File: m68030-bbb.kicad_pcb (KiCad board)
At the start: 4 copper layers, 177.8 x 127 mm, 13 parts, among them U1 MC68030, U10 M29F160F, U11 M29F160F, U12 XC95108TQ100, U13 SST39SF010, U2 R68561, U3 68230, U4 CY62167GN-45ZXI, U5 CY62167GN-45ZXI, U6 CY62167GN-45ZXI, U7 CY62167GN-45ZXI, U8 M29F160F, U9 M29F160F

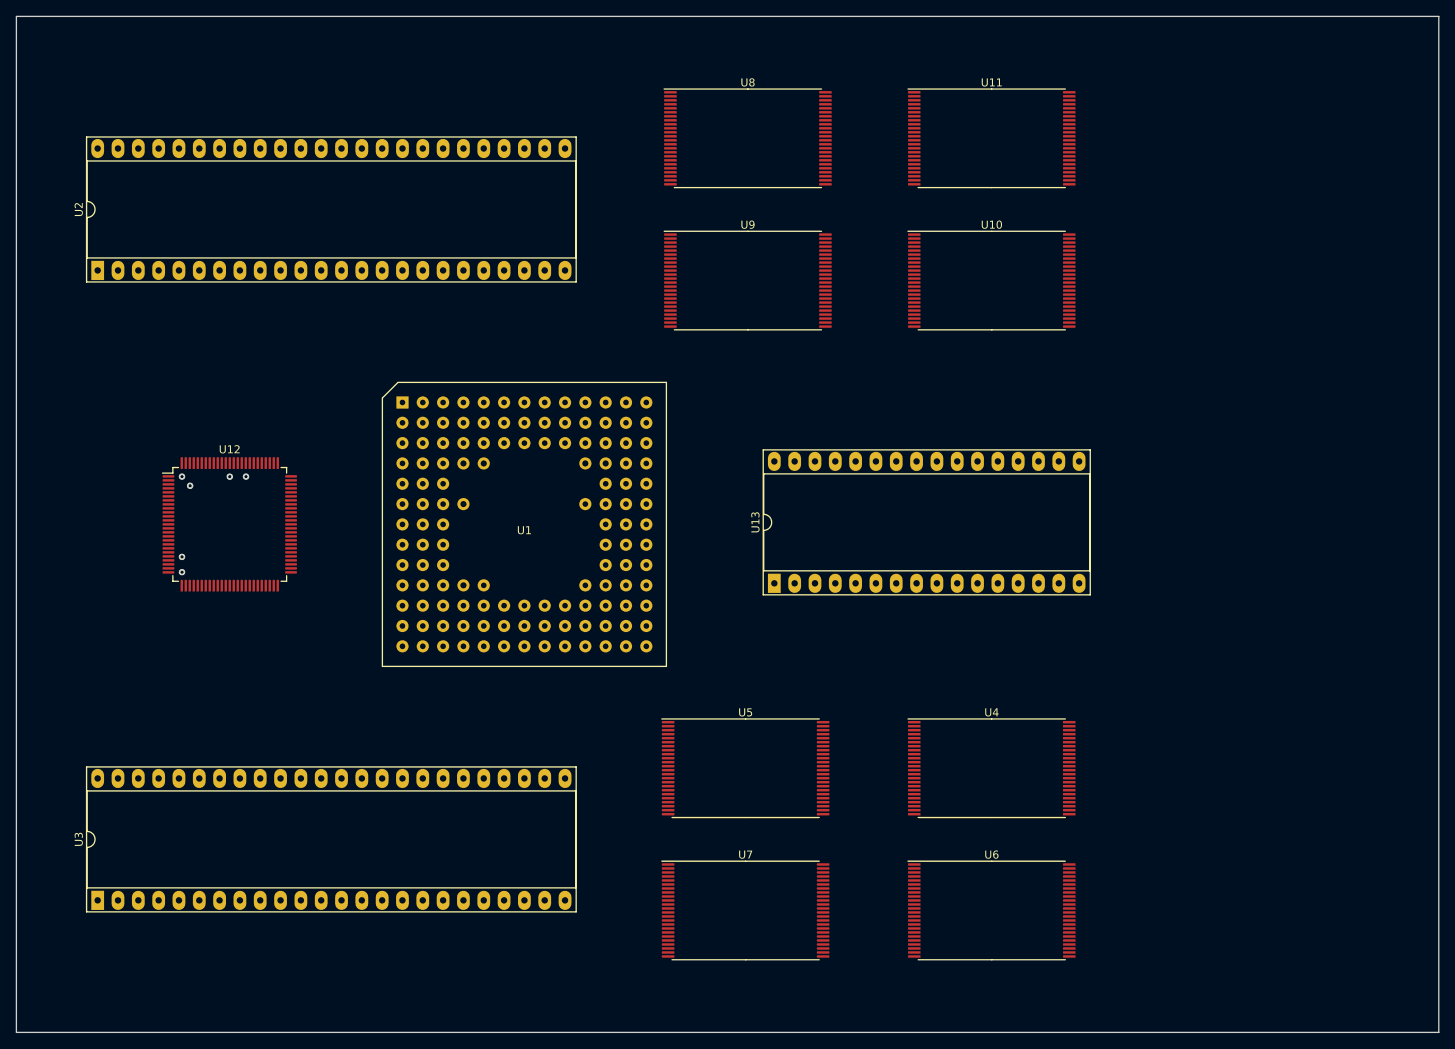
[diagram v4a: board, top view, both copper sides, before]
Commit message: Pretty much finished with the glue logic.  Doing intc now.
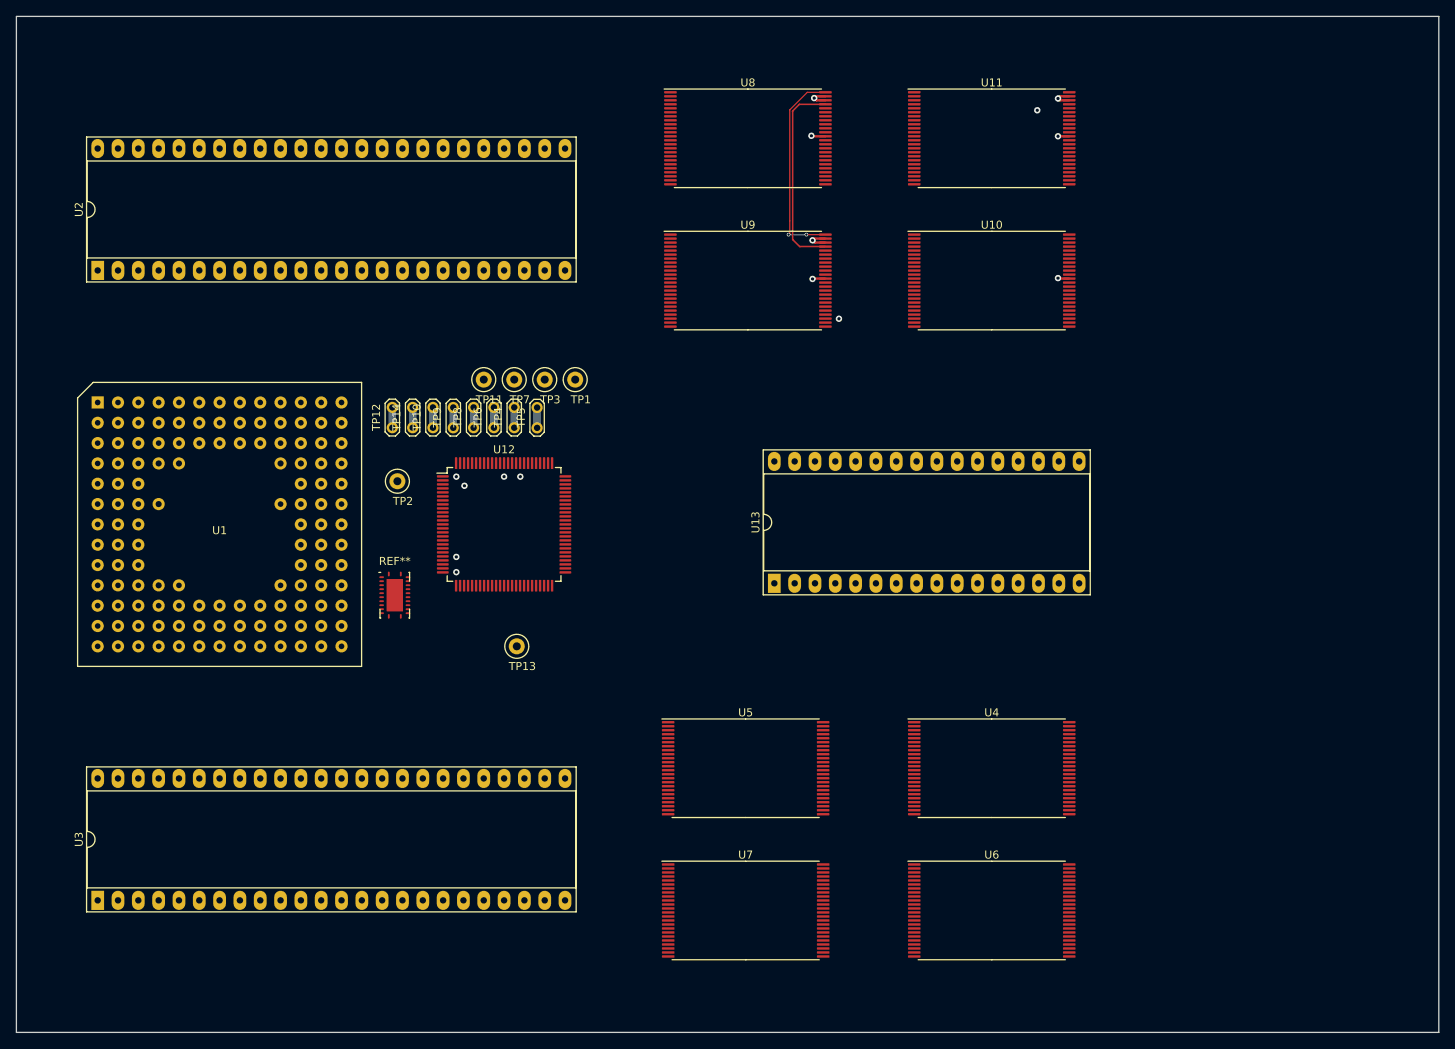
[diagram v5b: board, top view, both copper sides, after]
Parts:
- added REF**: VQFN-24_EP_3.4x5.4_Pitch0.5mm_RHL0024A, Rassilon:VQFN-24_EP_3.4x5.4_Pitch0.5mm_RHL0024A, F.Cu at (136.2, 91.4)
- added TP1: TestPoint_Small, TestPoint:TestPoint_Loop_D2.50mm_Drill1.0mm, F.Cu at (158.8, 64.5)
- added TP10: PGND, Rassilon:TestPoint_2Pads_Pitch2.54mm_Drill0.8mm_tie_bottom, F.Cu at (141.0, 70.5)
- added TP11: TestPoint_Small, TestPoint:TestPoint_Loop_D2.50mm_Drill1.0mm, F.Cu at (147.3, 64.5)
- added TP12: PGND, Rassilon:TestPoint_2Pads_Pitch2.54mm_Drill0.8mm_tie_bottom, F.Cu at (135.9, 70.5)
- added TP13: OCS, TestPoint:TestPoint_Loop_D2.50mm_Drill1.0mm, F.Cu at (151.4, 97.8)
- added TP14: PGND, Rassilon:TestPoint_2Pads_Pitch2.54mm_Drill0.8mm_tie_bottom, F.Cu at (138.4, 70.5)
- added TP2: TestPoint_Small, TestPoint:TestPoint_Loop_D2.50mm_Drill1.0mm, F.Cu at (136.5, 77.2)
- added TP3: PND, TestPoint:TestPoint_Loop_D2.50mm_Drill1.0mm, F.Cu at (154.9, 64.5)
- added TP4: PGND, Rassilon:TestPoint_2Pads_Pitch2.54mm_Drill0.8mm_tie_bottom, F.Cu at (151.1, 70.5)
- added TP5: PGND, Rassilon:TestPoint_2Pads_Pitch2.54mm_Drill0.8mm_tie_bottom, F.Cu at (154.0, 70.5)
- added TP6: PGND, Rassilon:TestPoint_2Pads_Pitch2.54mm_Drill0.8mm_tie_bottom, F.Cu at (148.6, 70.5)
- added TP7: TestPoint_Small, TestPoint:TestPoint_Loop_D2.50mm_Drill1.0mm, F.Cu at (151.1, 64.5)
- added TP8: PGND, Rassilon:TestPoint_2Pads_Pitch2.54mm_Drill0.8mm_tie_bottom, F.Cu at (146.1, 70.5)
- added TP9: PGND, Rassilon:TestPoint_2Pads_Pitch2.54mm_Drill0.8mm_tie_bottom, F.Cu at (143.5, 70.5)
- moved U1 38.1 mm to (114.3, 82.5)
- moved U12 34.3 mm to (149.9, 82.5)
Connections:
- net /SYSCLK2X renamed /~{CPUCLK}
- U10 pad 12: unconnected-(U10-Pad12) -> /~{RESET}
- U10 pad 37: unconnected-(U10-Pad37) -> +5V
- U10 pad 45: unconnected-(U10-Pad45) -> /A2
- U10 pad 47: unconnected-(U10-Pad47) -> GND
- U11 pad 12: unconnected-(U11-Pad12) -> /~{RESET}
- U11 pad 37: unconnected-(U11-Pad37) -> +5V
- U11 pad 45: unconnected-(U11-Pad45) -> /A2
- U11 pad 47: unconnected-(U11-Pad47) -> GND
- U12 pad 1: unconnected-(U12-Pad1) -> /~{RESET}
- U12 pad 11: unconnected-(U12-Pad11) -> /~{WR}
- U12 pad 12: unconnected-(U12-Pad12) -> /~{RD}
- U12 pad 15: /~{AS} -> /R/~{W}
- U12 pad 16: /~{DS} -> /~{CIIN}
- U12 pad 17: /R/~{W} -> /~{CIOUT}
- U12 pad 18: unconnected-(U12-Pad18) -> /~{DS}
- U12 pad 2: unconnected-(U12-Pad2) -> /~{IOSEL}
- U12 pad 23: /SYSCLK -> /~{AS}
- U12 pad 25: unconnected-(U12-Pad25) -> /A0
- U12 pad 28: unconnected-(U12-Pad28) -> /A1
- U12 pad 29: unconnected-(U12-Pad29) -> /~{RDUU}
- U12 pad 3: unconnected-(U12-Pad3) -> Net-(TP2-Pad1)
- U12 pad 30: unconnected-(U12-Pad30) -> /~{RDUM}
- U12 pad 32: unconnected-(U12-Pad32) -> /~{RDLM}
- U12 pad 33: unconnected-(U12-Pad33) -> /~{RDLL}
- U12 pad 34: unconnected-(U12-Pad34) -> /~{WEUU}
- U12 pad 35: unconnected-(U12-Pad35) -> /~{WEUM}
- U12 pad 36: unconnected-(U12-Pad36) -> /~{WELM}
- U12 pad 37: unconnected-(U12-Pad37) -> /~{WELL}
- U12 pad 39: unconnected-(U12-Pad39) -> /~{UDS}
- U12 pad 4: unconnected-(U12-Pad4) -> /~{IOSEL}
- U12 pad 40: unconnected-(U12-Pad40) -> /~{LDS}
- U12 pad 41: unconnected-(U12-Pad41) -> Net-(TP13-Pad1)
- U12 pad 42: unconnected-(U12-Pad42) -> /~{IOCS0}
- U12 pad 49: unconnected-(U12-Pad49) -> /~{IOCS1}
- U12 pad 65: unconnected-(U12-Pad65) -> /A20
- U12 pad 66: unconnected-(U12-Pad66) -> /A21
- U12 pad 67: unconnected-(U12-Pad67) -> /A22
- U12 pad 68: unconnected-(U12-Pad68) -> /A23
- U12 pad 70: unconnected-(U12-Pad70) -> /A24
- U12 pad 71: unconnected-(U12-Pad71) -> /A25
- U12 pad 72: unconnected-(U12-Pad72) -> /A26
- U12 pad 73: unconnected-(U12-Pad73) -> /A27
- U12 pad 74: unconnected-(U12-Pad74) -> /A28
- U12 pad 76: unconnected-(U12-Pad76) -> /A29
- U12 pad 77: unconnected-(U12-Pad77) -> /A30
- U12 pad 78: unconnected-(U12-Pad78) -> /A31
- U12 pad 79: unconnected-(U12-Pad79) -> Net-(TP1-Pad1)
- U12 pad 80: unconnected-(U12-Pad80) -> Net-(TP5-Pad1)
- U12 pad 81: unconnected-(U12-Pad81) -> Net-(TP3-Pad1)
- U12 pad 82: unconnected-(U12-Pad82) -> Net-(TP4-Pad1)
- U12 pad 85: unconnected-(U12-Pad85) -> Net-(TP6-Pad1)
- U12 pad 86: unconnected-(U12-Pad86) -> Net-(TP7-Pad1)
- U12 pad 87: unconnected-(U12-Pad87) -> Net-(TP8-Pad1)
- U12 pad 89: unconnected-(U12-Pad89) -> Net-(TP9-Pad1)
- U12 pad 90: unconnected-(U12-Pad90) -> Net-(TP10-Pad1)
- U12 pad 91: unconnected-(U12-Pad91) -> Net-(TP11-Pad1)
- U12 pad 92: unconnected-(U12-Pad92) -> Net-(TP14-Pad1)
- U12 pad 93: unconnected-(U12-Pad93) -> Net-(TP12-Pad1)
- U12 pad 94: unconnected-(U12-Pad94) -> /~{M230DTACK}
- U12 pad 95: unconnected-(U12-Pad95) -> /~{R561DTACK}
- U12 pad 96: unconnected-(U12-Pad96) -> /~{CBACK}
- U12 pad 97: unconnected-(U12-Pad97) -> /~{CBREQ}
- U13 pad 24: GND -> /~{RD}
- U13 pad 31: /R/~{W} -> /~{WR}
- U2 pad 1: unconnected-(U2-Pad1) -> /~{UDS}
- U2 pad 10: unconnected-(U2-Pad10) -> /A1
- U2 pad 12: unconnected-(U2-Pad12) -> /A4
- U2 pad 13: unconnected-(U2-Pad13) -> /A2
- U2 pad 14: unconnected-(U2-Pad14) -> /A3
- U2 pad 2: unconnected-(U2-Pad2) -> /~{R561DTACK}
- U2 pad 22: unconnected-(U2-Pad22) -> /R/~{W}
- U2 pad 31: unconnected-(U2-Pad31) -> /~{RESET}
- U2 pad 44: unconnected-(U2-Pad44) -> /~{R561CE}
- U2 pad 47: unconnected-(U2-Pad47) -> /~{LDS}
- U3 pad 1: unconnected-(U3-Pad1) -> /D29
- U3 pad 2: unconnected-(U3-Pad2) -> /D30
- U3 pad 25: unconnected-(U3-Pad25) -> /A4
- U3 pad 26: unconnected-(U3-Pad26) -> /A3
- U3 pad 27: unconnected-(U3-Pad27) -> /A2
- U3 pad 28: unconnected-(U3-Pad28) -> /A1
- U3 pad 29: unconnected-(U3-Pad29) -> /A0
- U3 pad 3: unconnected-(U3-Pad3) -> /D31
- U3 pad 38: unconnected-(U3-Pad38) -> GND
- U3 pad 39: unconnected-(U3-Pad39) -> /~{RESET}
- U3 pad 40: unconnected-(U3-Pad40) -> /CLK8MHz
- U3 pad 41: unconnected-(U3-Pad41) -> /~{M230CE}
- U3 pad 42: unconnected-(U3-Pad42) -> /~{M230DTACK}
- U3 pad 43: unconnected-(U3-Pad43) -> /R/~{W}
- U3 pad 44: unconnected-(U3-Pad44) -> /D24
- U3 pad 45: unconnected-(U3-Pad45) -> /D25
- U3 pad 46: unconnected-(U3-Pad46) -> /D26
- U3 pad 47: unconnected-(U3-Pad47) -> /D27
- U3 pad 48: unconnected-(U3-Pad48) -> /D28
- U4 pad 12: Net-(U4-Pad12) -> +5V
- U4 pad 14: Net-(U4-Pad12) -> +5V
- U4 pad 15: Net-(U4-Pad12) -> +5V
- U4 pad 37: unconnected-(U4-Pad37) -> +5V
- U5 pad 12: Net-(U5-Pad12) -> +5V
- U5 pad 14: Net-(U5-Pad12) -> +5V
- U5 pad 15: Net-(U5-Pad12) -> +5V
- U5 pad 37: unconnected-(U5-Pad37) -> +5V
- U6 pad 12: Net-(U6-Pad12) -> +5V
- U6 pad 14: Net-(U6-Pad12) -> +5V
- U6 pad 15: Net-(U6-Pad12) -> +5V
- U6 pad 37: unconnected-(U6-Pad37) -> +5V
- U7 pad 12: Net-(U7-Pad12) -> +5V
- U7 pad 14: Net-(U7-Pad12) -> +5V
- U7 pad 15: Net-(U7-Pad12) -> +5V
- U7 pad 37: unconnected-(U7-Pad37) -> +5V
- U8 pad 12: unconnected-(U8-Pad12) -> /~{RESET}
- U8 pad 37: unconnected-(U8-Pad37) -> +5V
- U8 pad 47: unconnected-(U8-Pad47) -> GND
- U9 pad 12: unconnected-(U9-Pad12) -> /~{RESET}
- U9 pad 37: unconnected-(U9-Pad37) -> +5V
- U9 pad 45: unconnected-(U9-Pad45) -> /A2
- U9 pad 47: unconnected-(U9-Pad47) -> GND
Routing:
- net /A19: track 0.00 -> 25.6 mm, vias 0 -> 2
- net /A2: track 0.00 -> 25.0 mm
- net GND: track 0.00 -> 9.47 mm, vias 3 -> 7
- net +5V: track 0.00 -> 6.25 mm, vias 3 -> 8
